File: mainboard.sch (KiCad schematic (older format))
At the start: 35 parts, among them J1 105017-1001, J2 Conn_01x04_Female, J3 Conn_01x02_Female, J4 Conn_01x09_Female, J5 Conn_01x02_Female, J6 Conn_01x02_Female, J7 Conn_01x04_Female, J8 Conn_01x03_Female, Q1 AOD4184A, U1 ESP32-WROOM-32E_(16MB)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

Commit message: diode opgezwierd
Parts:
- added D2: D, Diode_SMD:D_0805_2012Metric_Pad1.15x1.40mm_HandSolder, symbol Device:D
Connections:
- net 5V: now also D2.2 (A)
- net Mosfet_Out-: now also D2.1 (K)
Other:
- moved on the sheet: Q1, R5
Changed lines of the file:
@@
 RXD
-$Comp
-L mainboard-rescue:AOD4184A-AOD4184A Q1
-U 1 1 60421934
-P 8345 3105
-F 0 "Q1" H 8543 3151 50  0000 L CNN
-F 1 "AOD4184A" H 8543 3060 50  0000 L CNN
-F 2 "mylibs:DPAK228P994X240-4N" H 8345 3105 50  0001 L BNN
-F 3 "" H 8345 3105 50  0001 L BNN
-F 4 "2.4mm" H 8345 3105 50  0001 L BNN "MAXIMUM_PACKAGE_HEIGHT"
-F 5 "IPC-7351B" H 8345 3105 50  0001 L BNN "STANDARD"
-F 6 "0" H 8345 3105 50  0001 L BNN "PARTREV"
-F 7 "Alpha and Omega" H 8345 3105 50  0001 L BNN "MANUFACTURER"
-	1    8345 3105
-	1    0    0    -1
-$EndComp
-$Comp
-L Device:R R5
-U 1 1 6042498C
-P 8045 3805
-F 0 "R5" H 8115 3851 50  0000 L CNN
-F 1 "10K" H 8115 3760 50  0000 L CNN
-F 2 "Resistor_SMD:R_0805_2012Metric_Pad1.20x1.40mm_HandSolder" V 7975 3805 50  0001 C CNN
-F 3 "~" H 8045 3805 50  0001 C CNN
-	1    8045 3805
-	1    0    0    -1
-$EndComp
-Wire Wire Line
-	8245 3205 8245 3555
-Wire Wire Line
-	8245 3555 8045 3555
 $Comp
 L power:GND #PWR0106
 U 1 1 6042C92E
-P 8445 3305
-F 0 "#PWR0106" H 8445 3055 50  0001 C CNN
-F 1 "GND" H 8450 3132 50  0000 C CNN
-F 2 "" H 8445 3305 50  0001 C CNN
-F 3 "" H 8445 3305 50  0001 C CNN
-	1    8445 3305
-	1    0    0    -1
-$EndComp
-Wire Wire Line
-	8045 3655 8045 3555
-Connection ~ 8045 3555
+P 8150 3700
+F 0 "#PWR0106" H 8150 3450 50  0001 C CNN
+F 1 "GND" H 8155 3527 50  0000 C CNN
+F 2 "" H 8150 3700 50  0001 C CNN
+F 3 "" H 8150 3700 50  0001 C CNN
+	1    8150 3700
+	1    0    0    -1
+$EndComp
 $Comp
 L power:GND #PWR0108
 U 1 1 6042E2F0
-P 8045 3955
-F 0 "#PWR0108" H 8045 3705 50  0001 C CNN
-F 1 "GND" H 8050 3782 50  0000 C CNN
-F 2 "" H 8045 3955 50  0001 C CNN
-F 3 "" H 8045 3955 50  0001 C CNN
-	1    8045 3955
-	1    0    0    -1
-$EndComp
-Text GLabel 7895 3555 0    50   Input ~ 0
+P 7850 3950
+F 0 "#PWR0108" H 7850 3700 50  0001 C CNN
+F 1 "GND" H 7855 3777 50  0000 C CNN
+F 2 "" H 7850 3950 50  0001 C CNN
+F 3 "" H 7850 3950 50  0001 C CNN
+	1    7850 3950
+	1    0    0    -1
+$EndComp
+Text GLabel 7650 3600 0    50   Input ~ 0
 Mosfet_Trig
-Text GLabel 8245 2905 0    50   Input ~ 0
-Mosfet_Out-
-Wire Wire Line
-	8245 2905 8445 2905
 Text GLabel 9950 1400 2    50   Input ~ 0
 3V3
@@
 	1800 2650 2350 2650
 Connection ~ 1800 2650
-Wire Wire Line
-	7895 3555 8045 3555
 Text GLabel 1800 3150 0    50   Input ~ 0
 IRB
@@
 Text GLabel 2700 6400 0    50   Input ~ 0
 5V
+$Comp
+L mainboard-rescue:AOD4184A-AOD4184A Q1
+U 1 1 60421934
+P 8050 3500
+F 0 "Q1" H 8248 3546 50  0000 L CNN
+F 1 "AOD4184A" H 8248 3455 50  0000 L CNN
+F 2 "mylibs:DPAK228P994X240-4N" H 8050 3500 50  0001 L BNN
+F 3 "" H 8050 3500 50  0001 L BNN
+F 4 "2.4mm" H 8050 3500 50  0001 L BNN "MAXIMUM_PACKAGE_HEIGHT"
+F 5 "IPC-7351B" H 8050 3500 50  0001 L BNN "STANDARD"
+F 6 "0" H 8050 3500 50  0001 L BNN "PARTREV"
+F 7 "Alpha and Omega" H 8050 3500 50  0001 L BNN "MANUFACTURER"
+	1    8050 3500
+	1    0    0    -1
+$EndComp
+Text GLabel 7900 3200 0    50   Input ~ 0
+Mosfet_Out-
+$Comp
+L Device:R R5
+U 1 1 6042498C
+P 7850 3800
+F 0 "R5" H 7920 3846 50  0000 L CNN
+F 1 "10K" H 7920 3755 50  0000 L CNN
+F 2 "Resistor_SMD:R_0805_2012Metric_Pad1.20x1.40mm_HandSolder" V 7780 3800 50  0001 C CNN
+F 3 "~" H 7850 3800 50  0001 C CNN
+	1    7850 3800
+	1    0    0    -1
+$EndComp
+Wire Wire Line
+	7650 3600 7850 3600
+Wire Wire Line
+	7850 3600 7850 3650
+Wire Wire Line
+	7850 3600 7950 3600
+Connection ~ 7850 3600
+Wire Wire Line
+	8150 3300 8150 3200
+Wire Wire Line
+	8150 3200 7900 3200
+Text GLabel 8150 2900 0    50   Input ~ 0
+5V
+Connection ~ 8150 3200
+$Comp
+L Device:D D2
+U 1 1 606F85FC
+P 8150 3050
+F 0 "D2" V 8196 2970 50  0000 R CNN
+F 1 "D" V 8105 2970 50  0000 R CNN
+F 2 "Diode_SMD:D_0805_2012Metric_Pad1.15x1.40mm_HandSolder" H 8150 3050 50  0001 C CNN
+F 3 "~" H 8150 3050 50  0001 C CNN
+	1    8150 3050
+	0    -1   -1   0
+$EndComp
 $EndSCHEMATC

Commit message: Revert "diode opgezwierd"
This reverts commit 37b3bf43883e8e94795329db478c9cb5caa1757c.
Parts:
- removed D2: D, Diode_SMD:D_0805_2012Metric_Pad1.15x1.40mm_HandSolder, symbol Device:D
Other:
- moved on the sheet: Q1, R5
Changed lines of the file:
@@
 RXD
+$Comp
+L mainboard-rescue:AOD4184A-AOD4184A Q1
+U 1 1 60421934
+P 8345 3105
+F 0 "Q1" H 8543 3151 50  0000 L CNN
+F 1 "AOD4184A" H 8543 3060 50  0000 L CNN
+F 2 "mylibs:DPAK228P994X240-4N" H 8345 3105 50  0001 L BNN
+F 3 "" H 8345 3105 50  0001 L BNN
+F 4 "2.4mm" H 8345 3105 50  0001 L BNN "MAXIMUM_PACKAGE_HEIGHT"
+F 5 "IPC-7351B" H 8345 3105 50  0001 L BNN "STANDARD"
+F 6 "0" H 8345 3105 50  0001 L BNN "PARTREV"
+F 7 "Alpha and Omega" H 8345 3105 50  0001 L BNN "MANUFACTURER"
+	1    8345 3105
+	1    0    0    -1
+$EndComp
+$Comp
+L Device:R R5
+U 1 1 6042498C
+P 8045 3805
+F 0 "R5" H 8115 3851 50  0000 L CNN
+F 1 "10K" H 8115 3760 50  0000 L CNN
+F 2 "Resistor_SMD:R_0805_2012Metric_Pad1.20x1.40mm_HandSolder" V 7975 3805 50  0001 C CNN
+F 3 "~" H 8045 3805 50  0001 C CNN
+	1    8045 3805
+	1    0    0    -1
+$EndComp
+Wire Wire Line
+	8245 3205 8245 3555
+Wire Wire Line
+	8245 3555 8045 3555
 $Comp
 L power:GND #PWR0106
 U 1 1 6042C92E
-P 8150 3700
-F 0 "#PWR0106" H 8150 3450 50  0001 C CNN
-F 1 "GND" H 8155 3527 50  0000 C CNN
-F 2 "" H 8150 3700 50  0001 C CNN
-F 3 "" H 8150 3700 50  0001 C CNN
-	1    8150 3700
-	1    0    0    -1
-$EndComp
+P 8445 3305
+F 0 "#PWR0106" H 8445 3055 50  0001 C CNN
+F 1 "GND" H 8450 3132 50  0000 C CNN
+F 2 "" H 8445 3305 50  0001 C CNN
+F 3 "" H 8445 3305 50  0001 C CNN
+	1    8445 3305
+	1    0    0    -1
+$EndComp
+Wire Wire Line
+	8045 3655 8045 3555
+Connection ~ 8045 3555
 $Comp
 L power:GND #PWR0108
 U 1 1 6042E2F0
-P 7850 3950
-F 0 "#PWR0108" H 7850 3700 50  0001 C CNN
-F 1 "GND" H 7855 3777 50  0000 C CNN
-F 2 "" H 7850 3950 50  0001 C CNN
-F 3 "" H 7850 3950 50  0001 C CNN
-	1    7850 3950
-	1    0    0    -1
-$EndComp
-Text GLabel 7650 3600 0    50   Input ~ 0
+P 8045 3955
+F 0 "#PWR0108" H 8045 3705 50  0001 C CNN
+F 1 "GND" H 8050 3782 50  0000 C CNN
+F 2 "" H 8045 3955 50  0001 C CNN
+F 3 "" H 8045 3955 50  0001 C CNN
+	1    8045 3955
+	1    0    0    -1
+$EndComp
+Text GLabel 7895 3555 0    50   Input ~ 0
 Mosfet_Trig
+Text GLabel 8245 2905 0    50   Input ~ 0
+Mosfet_Out-
+Wire Wire Line
+	8245 2905 8445 2905
 Text GLabel 9950 1400 2    50   Input ~ 0
 3V3
@@
 	1800 2650 2350 2650
 Connection ~ 1800 2650
+Wire Wire Line
+	7895 3555 8045 3555
 Text GLabel 1800 3150 0    50   Input ~ 0
 IRB
@@
 Text GLabel 2700 6400 0    50   Input ~ 0
 5V
-$Comp
-L mainboard-rescue:AOD4184A-AOD4184A Q1
-U 1 1 60421934
-P 8050 3500
-F 0 "Q1" H 8248 3546 50  0000 L CNN
-F 1 "AOD4184A" H 8248 3455 50  0000 L CNN
-F 2 "mylibs:DPAK228P994X240-4N" H 8050 3500 50  0001 L BNN
-F 3 "" H 8050 3500 50  0001 L BNN
-F 4 "2.4mm" H 8050 3500 50  0001 L BNN "MAXIMUM_PACKAGE_HEIGHT"
-F 5 "IPC-7351B" H 8050 3500 50  0001 L BNN "STANDARD"
-F 6 "0" H 8050 3500 50  0001 L BNN "PARTREV"
-F 7 "Alpha and Omega" H 8050 3500 50  0001 L BNN "MANUFACTURER"
-	1    8050 3500
-	1    0    0    -1
-$EndComp
-Text GLabel 7900 3200 0    50   Input ~ 0
-Mosfet_Out-
-$Comp
-L Device:R R5
-U 1 1 6042498C
-P 7850 3800
-F 0 "R5" H 7920 3846 50  0000 L CNN
-F 1 "10K" H 7920 3755 50  0000 L CNN
-F 2 "Resistor_SMD:R_0805_2012Metric_Pad1.20x1.40mm_HandSolder" V 7780 3800 50  0001 C CNN
-F 3 "~" H 7850 3800 50  0001 C CNN
-	1    7850 3800
-	1    0    0    -1
-$EndComp
-Wire Wire Line
-	7650 3600 7850 3600
-Wire Wire Line
-	7850 3600 7850 3650
-Wire Wire Line
-	7850 3600 7950 3600
-Connection ~ 7850 3600
-Wire Wire Line
-	8150 3300 8150 3200
-Wire Wire Line
-	8150 3200 7900 3200
-Text GLabel 8150 2900 0    50   Input ~ 0
-5V
-Connection ~ 8150 3200
-$Comp
-L Device:D D2
-U 1 1 606F85FC
-P 8150 3050
-F 0 "D2" V 8196 2970 50  0000 R CNN
-F 1 "D" V 8105 2970 50  0000 R CNN
-F 2 "Diode_SMD:D_0805_2012Metric_Pad1.15x1.40mm_HandSolder" H 8150 3050 50  0001 C CNN
-F 3 "~" H 8150 3050 50  0001 C CNN
-	1    8150 3050
-	0    -1   -1   0
-$EndComp
 $EndSCHEMATC

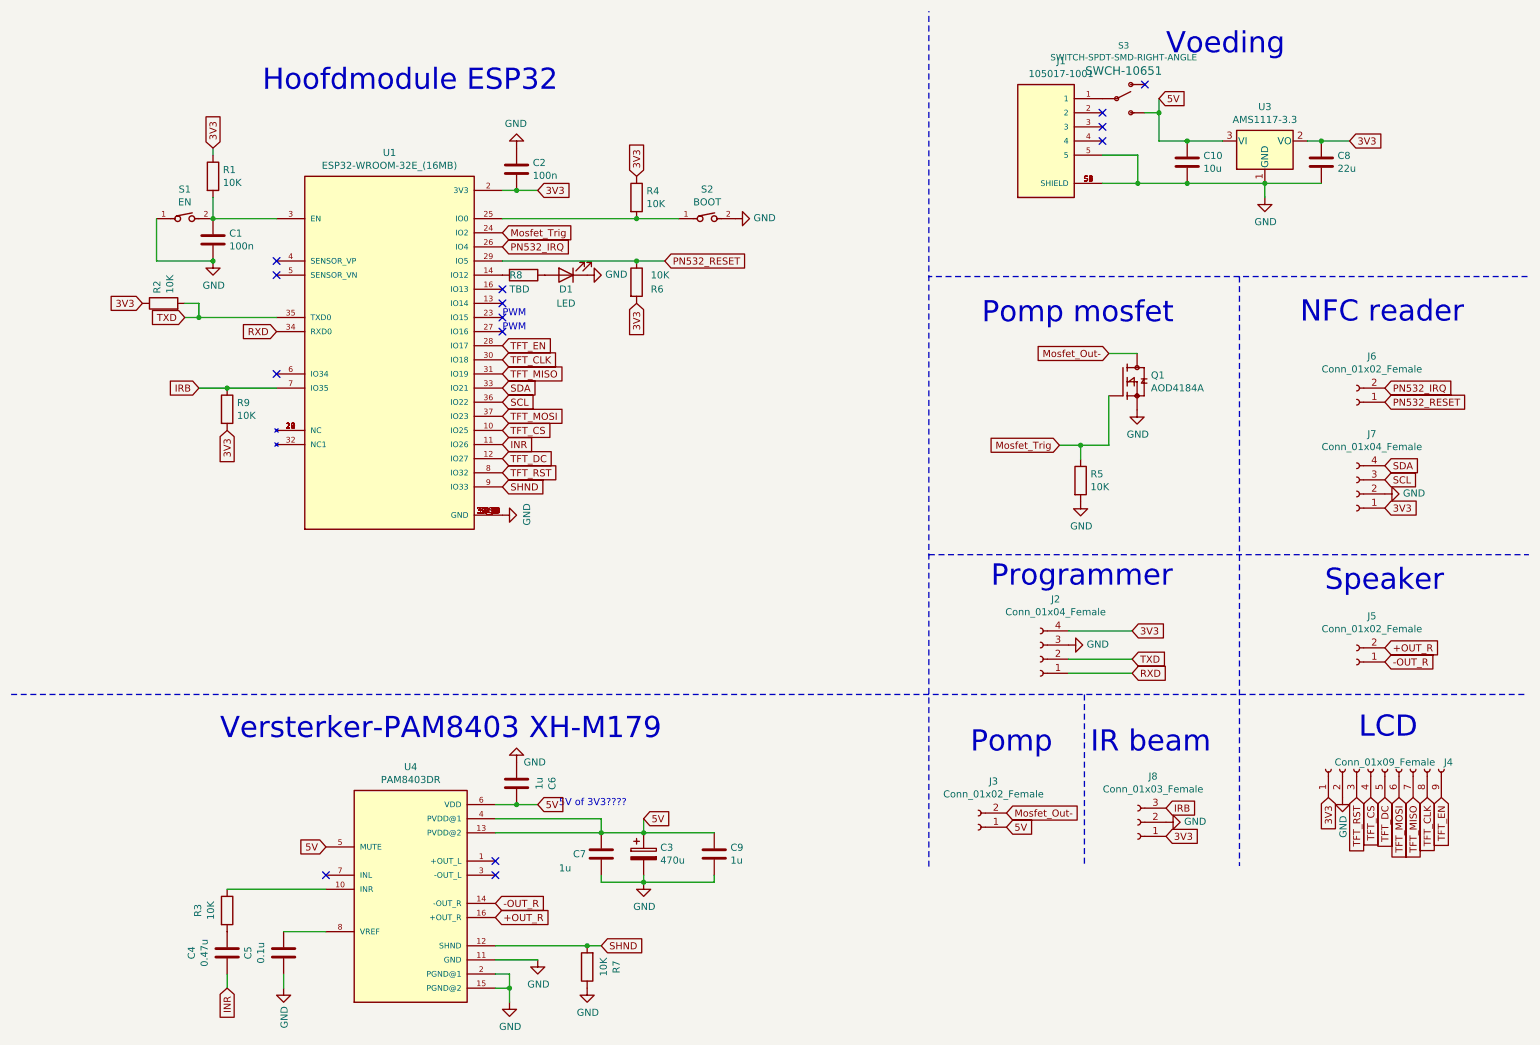
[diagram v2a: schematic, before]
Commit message: amai ik ben er een boeltje van aan het maken
flyback diode toegevoegd
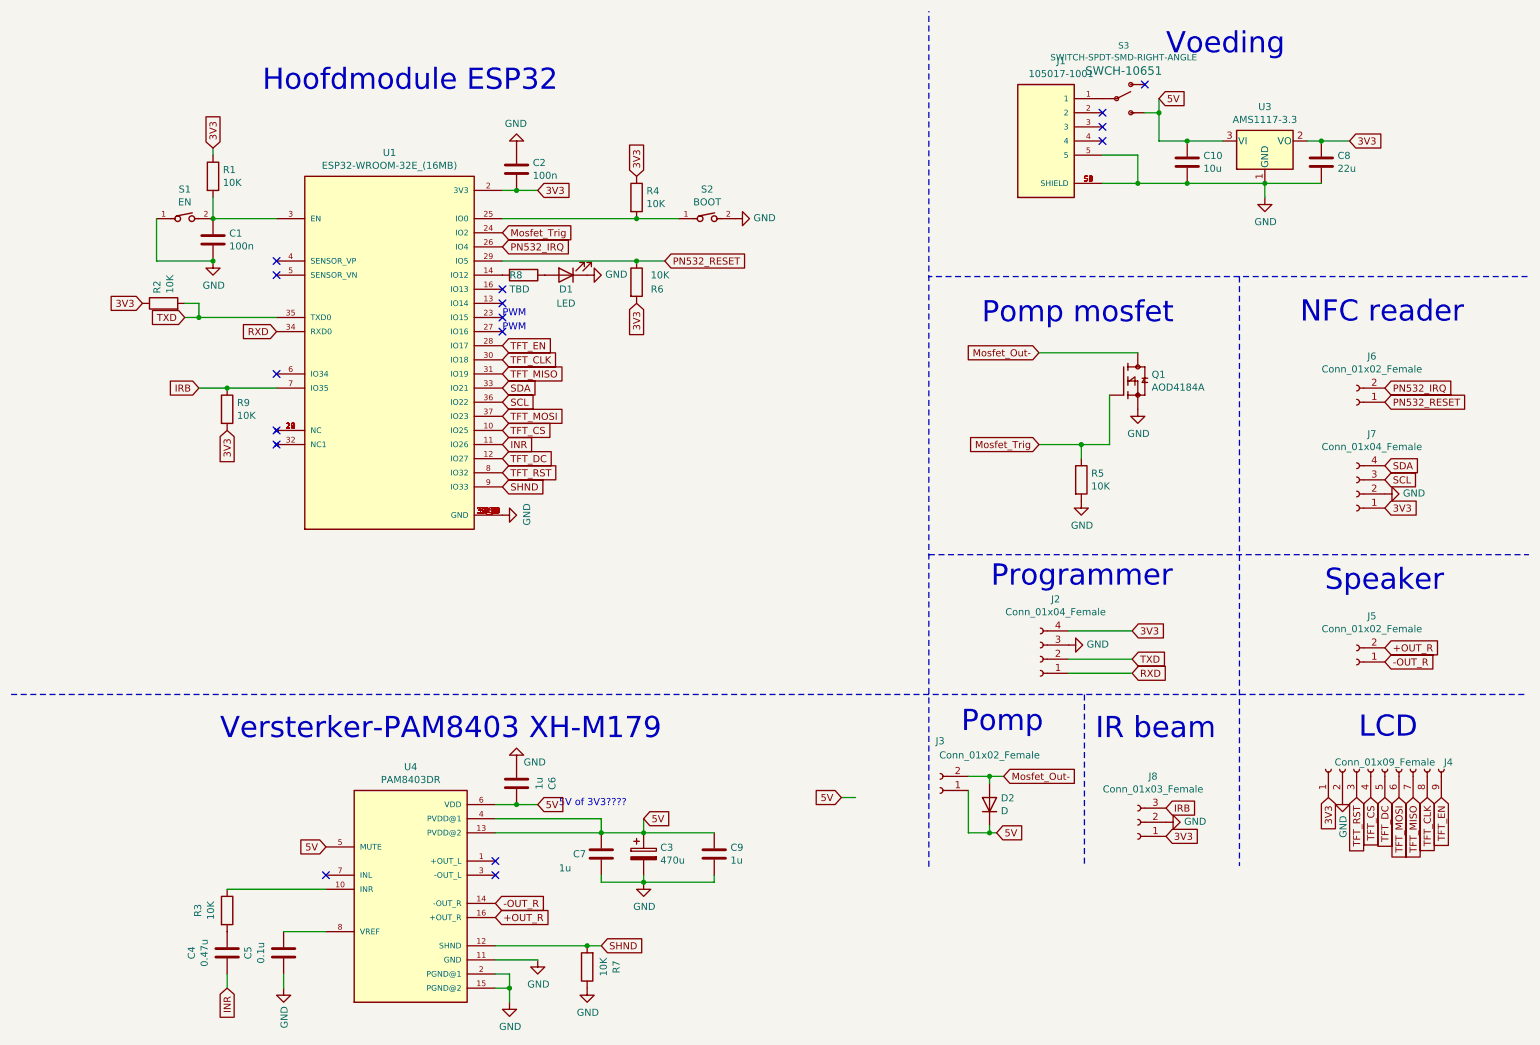
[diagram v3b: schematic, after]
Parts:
- added D2: D, Diode_SMD:D_0805_2012Metric_Pad1.15x1.40mm_HandSolder, symbol Device:D
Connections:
- net 5V: now also D2.1 (K)
- net Mosfet_Out-: now also D2.2 (A)
- no-connect marks 14 -> 16
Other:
- moved on the sheet: J3
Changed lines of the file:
@@
 RXD
-$Comp
-L mainboard-rescue:AOD4184A-AOD4184A Q1
-U 1 1 60421934
-P 8345 3105
-F 0 "Q1" H 8543 3151 50  0000 L CNN
-F 1 "AOD4184A" H 8543 3060 50  0000 L CNN
-F 2 "mylibs:DPAK228P994X240-4N" H 8345 3105 50  0001 L BNN
-F 3 "" H 8345 3105 50  0001 L BNN
-F 4 "2.4mm" H 8345 3105 50  0001 L BNN "MAXIMUM_PACKAGE_HEIGHT"
-F 5 "IPC-7351B" H 8345 3105 50  0001 L BNN "STANDARD"
-F 6 "0" H 8345 3105 50  0001 L BNN "PARTREV"
-F 7 "Alpha and Omega" H 8345 3105 50  0001 L BNN "MANUFACTURER"
-	1    8345 3105
-	1    0    0    -1
-$EndComp
 $Comp
 L Device:R R5
 U 1 1 6042498C
-P 8045 3805
-F 0 "R5" H 8115 3851 50  0000 L CNN
-F 1 "10K" H 8115 3760 50  0000 L CNN
-F 2 "Resistor_SMD:R_0805_2012Metric_Pad1.20x1.40mm_HandSolder" V 7975 3805 50  0001 C CNN
-F 3 "~" H 8045 3805 50  0001 C CNN
-	1    8045 3805
-	1    0    0    -1
-$EndComp
-Wire Wire Line
-	8245 3205 8245 3555
-Wire Wire Line
-	8245 3555 8045 3555
+P 8050 3800
+F 0 "R5" H 8120 3846 50  0000 L CNN
+F 1 "10K" H 8120 3755 50  0000 L CNN
+F 2 "Resistor_SMD:R_0805_2012Metric_Pad1.20x1.40mm_HandSolder" V 7980 3800 50  0001 C CNN
+F 3 "~" H 8050 3800 50  0001 C CNN
+	1    8050 3800
+	1    0    0    -1
+$EndComp
 $Comp
 L power:GND #PWR0106
 U 1 1 6042C92E
-P 8445 3305
-F 0 "#PWR0106" H 8445 3055 50  0001 C CNN
-F 1 "GND" H 8450 3132 50  0000 C CNN
-F 2 "" H 8445 3305 50  0001 C CNN
-F 3 "" H 8445 3305 50  0001 C CNN
-	1    8445 3305
-	1    0    0    -1
-$EndComp
-Wire Wire Line
-	8045 3655 8045 3555
-Connection ~ 8045 3555
+P 8450 3300
+F 0 "#PWR0106" H 8450 3050 50  0001 C CNN
+F 1 "GND" H 8455 3127 50  0000 C CNN
+F 2 "" H 8450 3300 50  0001 C CNN
+F 3 "" H 8450 3300 50  0001 C CNN
+	1    8450 3300
+	1    0    0    -1
+$EndComp
 $Comp
 L power:GND #PWR0108
 U 1 1 6042E2F0
-P 8045 3955
-F 0 "#PWR0108" H 8045 3705 50  0001 C CNN
-F 1 "GND" H 8050 3782 50  0000 C CNN
-F 2 "" H 8045 3955 50  0001 C CNN
-F 3 "" H 8045 3955 50  0001 C CNN
-	1    8045 3955
-	1    0    0    -1
-$EndComp
-Text GLabel 7895 3555 0    50   Input ~ 0
+P 8050 3950
+F 0 "#PWR0108" H 8050 3700 50  0001 C CNN
+F 1 "GND" H 8055 3777 50  0000 C CNN
+F 2 "" H 8050 3950 50  0001 C CNN
+F 3 "" H 8050 3950 50  0001 C CNN
+	1    8050 3950
+	1    0    0    -1
+$EndComp
+Text GLabel 7750 3550 0    50   Input ~ 0
 Mosfet_Trig
-Text GLabel 8245 2905 0    50   Input ~ 0
-Mosfet_Out-
-Wire Wire Line
-	8245 2905 8445 2905
 Text GLabel 9950 1400 2    50   Input ~ 0
 3V3
@@
 	1800 2650 2350 2650
 Connection ~ 1800 2650
-Wire Wire Line
-	7895 3555 8045 3555
 Text GLabel 1800 3150 0    50   Input ~ 0
 IRB
@@
 TFT_MISO
 NoConn ~ 2700 6600
-Text Notes 7265 5745 0    150  ~ 0
+Text Notes 7200 5600 0    150  ~ 0
 Pomp
 $Comp
 L Connector:Conn_01x02_Female J3
 U 1 1 6053B267
-P 7320 6260
-F 0 "J3" H 7212 5935 50  0000 C CNN
-F 1 "Conn_01x02_Female" H 7212 6026 50  0000 C CNN
-F 2 "Connector_PinSocket_2.54mm:PinSocket_1x02_P2.54mm_Vertical" H 7320 6260 50  0001 C CNN
-F 3 "~" H 7320 6260 50  0001 C CNN
-	1    7320 6260
-	-1   0    0    1
-$EndComp
-Text GLabel 7520 6160 2    50   Input ~ 0
+P 7050 6000
+F 0 "J3" H 7050 5650 50  0000 C CNN
+F 1 "Conn_01x02_Female" H 6700 5750 50  0000 C CNN
+F 2 "Connector_PinSocket_2.54mm:PinSocket_1x02_P2.54mm_Vertical" H 7050 6000 50  0001 C CNN
+F 3 "~" H 7050 6000 50  0001 C CNN
+	1    7050 6000
+	-1   0    0    1
+$EndComp
+Text GLabel 7500 5900 2    50   Input ~ 0
 Mosfet_Out-
-Text GLabel 7520 6260 2    50   Input ~ 0
+Text GLabel 7450 6300 2    50   Input ~ 0
 5V
 Text Notes 9775 4600 0    150  ~ 0
@@
 Wire Wire Line
 	8600 1100 8600 1200
-Text Notes 8115 5745 0    150  ~ 0
+Text Notes 8150 5650 0    150  ~ 0
 IR beam
 $Comp
@@
 Text GLabel 2700 6400 0    50   Input ~ 0
 5V
+Text GLabel 7750 2900 0    50   Input ~ 0
+Mosfet_Out-
+$Comp
+L mainboard-rescue:AOD4184A-AOD4184A Q1
+U 1 1 60421934
+P 8350 3100
+F 0 "Q1" H 8548 3146 50  0000 L CNN
+F 1 "AOD4184A" H 8548 3055 50  0000 L CNN
+F 2 "mylibs:DPAK228P994X240-4N" H 8350 3100 50  0001 L BNN
+F 3 "" H 8350 3100 50  0001 L BNN
+F 4 "2.4mm" H 8350 3100 50  0001 L BNN "MAXIMUM_PACKAGE_HEIGHT"
+F 5 "IPC-7351B" H 8350 3100 50  0001 L BNN "STANDARD"
+F 6 "0" H 8350 3100 50  0001 L BNN "PARTREV"
+F 7 "Alpha and Omega" H 8350 3100 50  0001 L BNN "MANUFACTURER"
+	1    8350 3100
+	1    0    0    -1
+$EndComp
+Wire Wire Line
+	7750 3550 8050 3550
+Wire Wire Line
+	8250 3550 8250 3200
+Wire Wire Line
+	8050 3650 8050 3550
+Connection ~ 8050 3550
+Wire Wire Line
+	8050 3550 8250 3550
+Text GLabel 6350 6050 0    50   Input ~ 0
+5V
+$Comp
+L Device:D D2
+U 1 1 60703FAA
+P 7400 6100
+F 0 "D2" V 7446 6020 50  0000 R CNN
+F 1 "D" V 7355 6020 50  0000 R CNN
+F 2 "Diode_SMD:D_0805_2012Metric_Pad1.15x1.40mm_HandSolder" H 7400 6100 50  0001 C CNN
+F 3 "~" H 7400 6100 50  0001 C CNN
+	1    7400 6100
+	0    -1   -1   0
+$EndComp
+Wire Wire Line
+	6350 6050 6450 6050
+Wire Wire Line
+	7750 2900 8450 2900
+Wire Wire Line
+	7250 5900 7400 5900
+Connection ~ 7400 5900
+Wire Wire Line
+	7400 5900 7500 5900
+Wire Wire Line
+	7250 6300 7400 6300
+Wire Wire Line
+	7250 6000 7250 6300
+Wire Wire Line
+	7400 5900 7400 5950
+Wire Wire Line
+	7400 6250 7400 6300
+Connection ~ 7400 6300
+Wire Wire Line
+	7400 6300 7450 6300
+NoConn ~ 2350 3550
+NoConn ~ 2350 3450
 $EndSCHEMATC

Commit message: de woordjes staan mooier nu
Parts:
- S1, S2: symbol 434111043826:434111043826 -> mainboard-rescue:434111043826-434111043826
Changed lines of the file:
@@
 $EndComp
 $Comp
-L 434111043826:434111043826 S2
+L mainboard-rescue:434111043826-434111043826 S2
 U 1 1 6040FDB7
 P 5400 1950
@@
 $EndComp
 $Comp
-L 434111043826:434111043826 S1
+L mainboard-rescue:434111043826-434111043826 S1
 U 1 1 6040F46E
 P 1700 1950
